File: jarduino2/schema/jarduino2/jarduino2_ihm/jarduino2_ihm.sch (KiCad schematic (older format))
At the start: 18 parts, among them J1 Alim CPU, J2 Alim CPU, J3 Indicateurs, J4 Pompes, SW1 Pile On/Off, SW2 POW ON/OFF, SW3 Pile On/Off, SW4 Pompe 1, SW5 Pompe 2

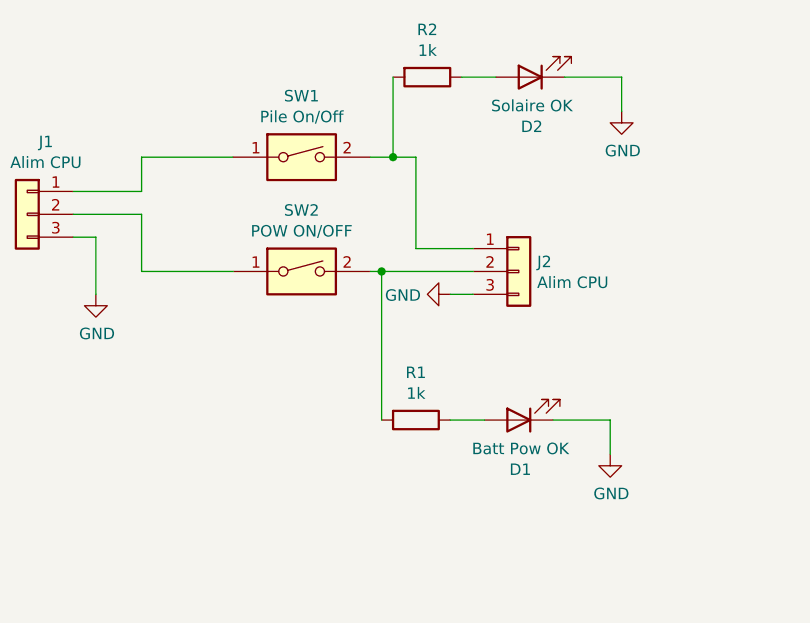
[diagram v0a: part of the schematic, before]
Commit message: Amélioration proto: - Diametre trous de fixation 4mm (avec compo sepcial) - SW1/SW2 echanges Batt/Sol
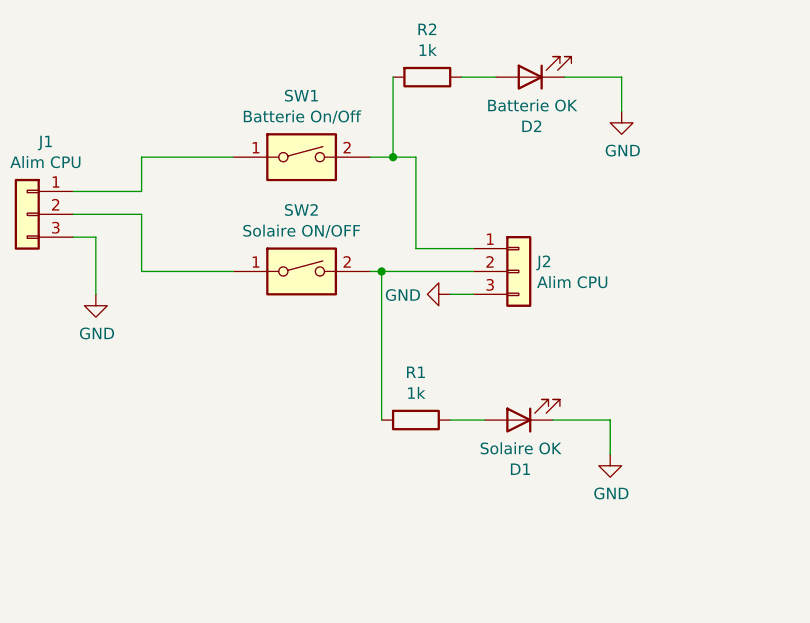
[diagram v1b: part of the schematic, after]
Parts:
- D1: value Batt Pow OK -> Solaire OK
- D2: value Solaire OK -> Batterie OK
- SW1: value Pile On/Off -> Batterie On/Off
- SW2: value POW ON/OFF -> Solaire ON/OFF
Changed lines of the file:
@@
 P 2150 2150
 F 0 "SW2" H 2150 2417 50  0000 C CNN
-F 1 "POW ON/OFF" H 2150 2326 50  0000 C CNN
+F 1 "Solaire ON/OFF" H 2150 2326 50  0000 C CNN
 F 2 "Connector_PinHeader_2.54mm:PinHeader_1x02_P2.54mm_Vertical" H 2150 2150 50  0001 C CNN
 F 3 "~" H 2150 2150 50  0001 C CNN
@@
 P 2150 1650
 F 0 "SW1" H 2150 1917 50  0000 C CNN
-F 1 "Pile On/Off" H 2150 1826 50  0000 C CNN
+F 1 "Batterie On/Off" H 2150 1826 50  0000 C CNN
 F 2 "Connector_PinHeader_2.54mm:PinHeader_1x02_P2.54mm_Vertical" H 2150 1650 50  0001 C CNN
 F 3 "~" H 2150 1650 50  0001 C CNN
@@
 P 3150 1300
 F 0 "D2" H 3143 1517 50  0000 C CNN
-F 1 "Solaire OK" H 3143 1426 50  0000 C CNN
+F 1 "Batterie OK" H 3143 1426 50  0000 C CNN
 F 2 "LED_THT:LED_D3.0mm_Clear" H 3150 1300 50  0001 C CNN
 F 3 "~" H 3150 1300 50  0001 C CNN
@@
 P 3100 2800
 F 0 "D1" H 3093 3017 50  0000 C CNN
-F 1 "Batt Pow OK" H 3093 2926 50  0000 C CNN
+F 1 "Solaire OK" H 3093 2926 50  0000 C CNN
 F 2 "LED_THT:LED_D3.0mm_Clear" H 3100 2800 50  0001 C CNN
 F 3 "~" H 3100 2800 50  0001 C CNN
